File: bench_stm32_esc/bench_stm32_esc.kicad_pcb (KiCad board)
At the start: 4 copper layers, 117 x 75 mm, 107 parts, among them CN1 S6B-PH-K-S-, CN10 Conn_02x19_Odd_Even, CN7 Conn_02x19_Odd_Even, J1 XT60PW-M, Q1 CSD19532Q5B, Q2 CSD19532Q5B, Q3 CSD19532Q5B, Q4 CSD19532Q5B, Q5 CSD19532Q5B, Q6 CSD19532Q5B, U1 DRV8353RSRGZT, U2 AMS1117, U3 TPD1E05U06DYA, U4 MR60PW-M.G.B, U7 TB60

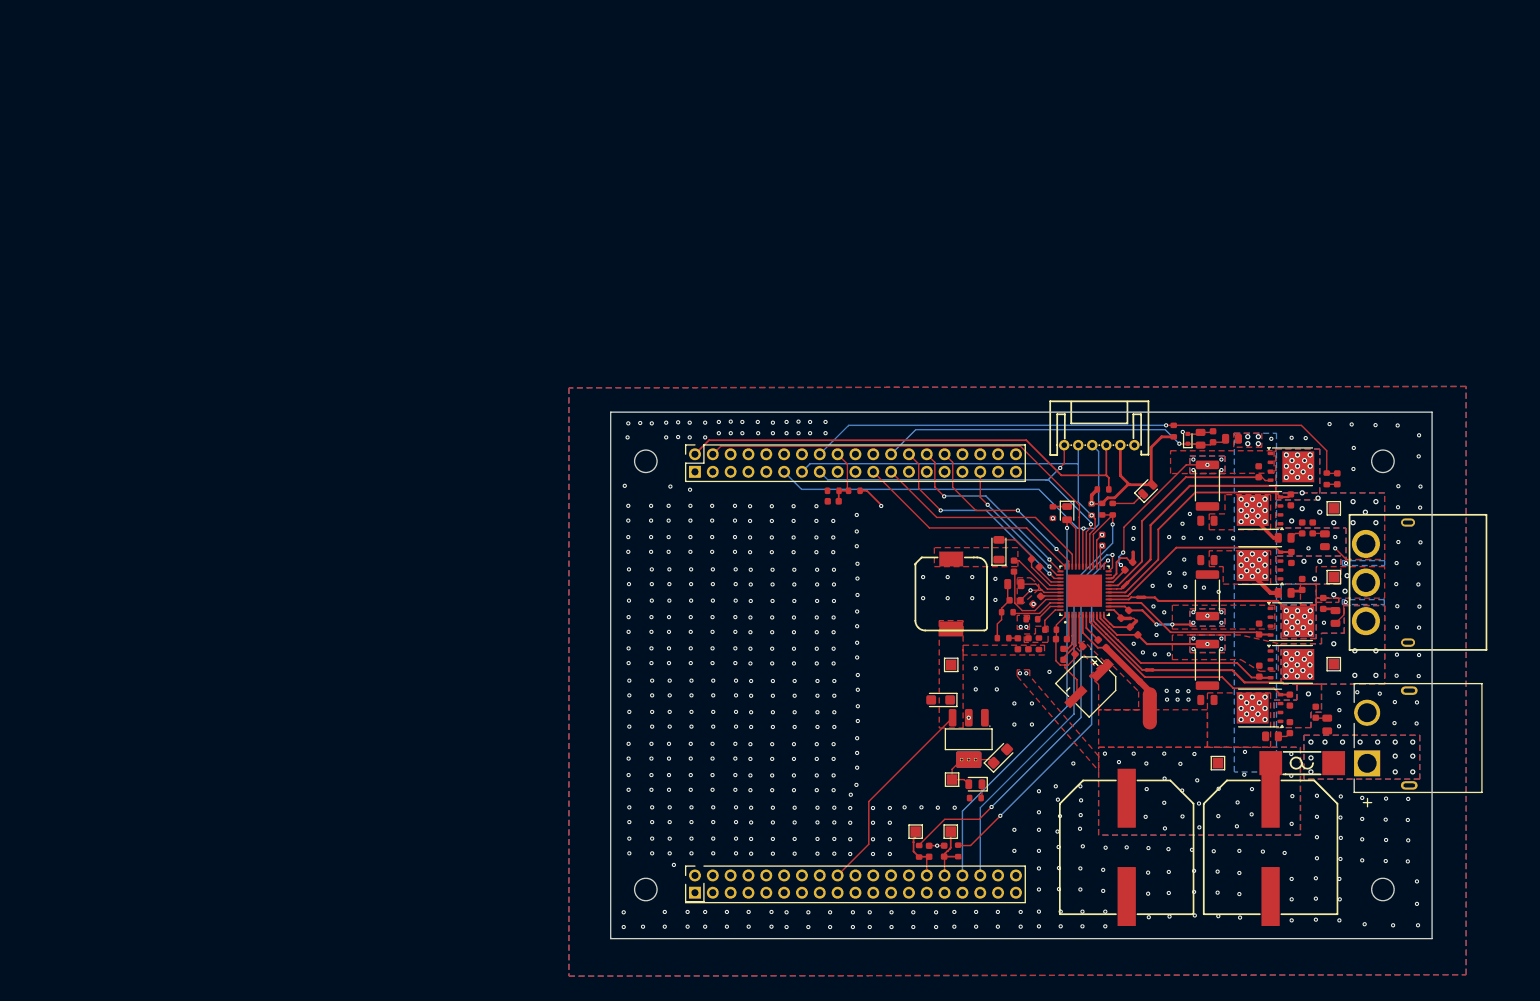
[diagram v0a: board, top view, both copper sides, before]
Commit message: Added smd stm32
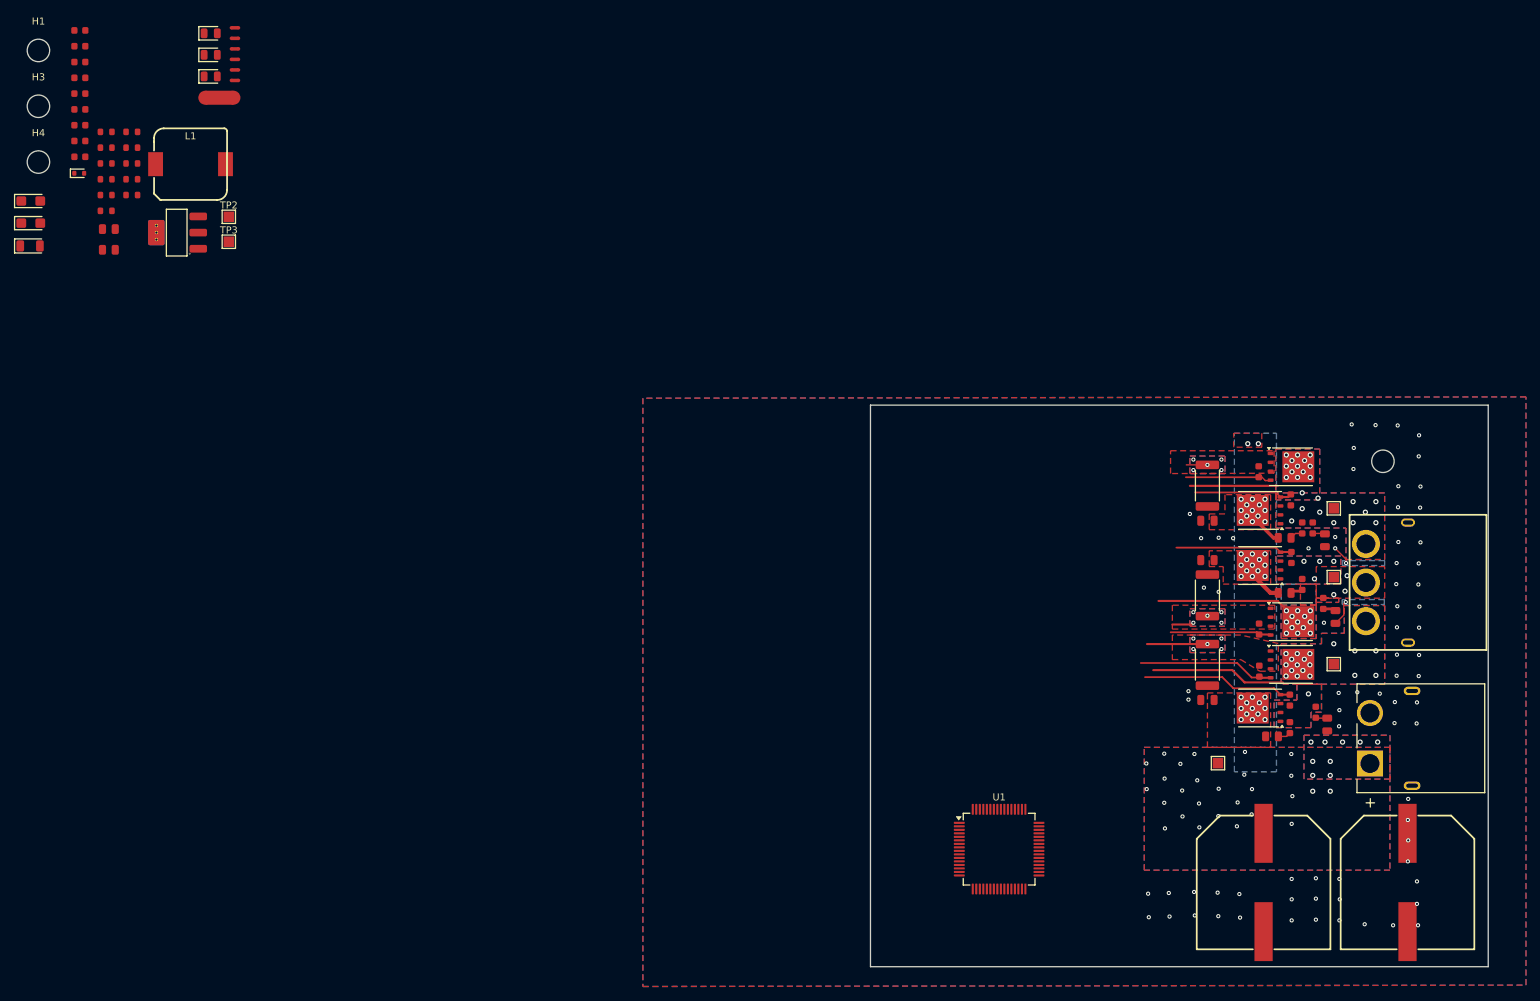
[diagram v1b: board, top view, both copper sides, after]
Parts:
- removed C1, C2, C3, C4: 1uF, PCM_JLCPCB:C_0603
- removed C16: VT10UF100V167RV0127, footprints:VT10UF100V167RV0127
- removed C34, C35: 2.2nF, PCM_JLCPCB:C_0603
- removed C5, C8, C9: 100nF, PCM_JLCPCB:C_0603
- removed C6: 47nF, PCM_JLCPCB:C_0603
- removed C7: 1uF, PCM_JLCPCB:C_0805
- removed CN1: S6B-PH-K-S-, footprints:S6B-PH-K-S(LF)(SN)
- removed CN10, CN7: Conn_02x19_Odd_Even, Connector_PinSocket_2.54mm:PinSocket_2x19_P2.54mm_Vertical
- removed R1: 100kΩ, PCM_JLCPCB:R_0603
- removed R15, R16: 56Ω, PCM_JLCPCB:R_0603
- removed R17: 1kΩ, PCM_JLCPCB:R_0603
- removed R2: 274kΩ, PCM_JLCPCB:R_0603
- removed R25: 10kΩ, PCM_JLCPCB:R_0603
- removed TP4, TP5: TestPoint, TestPoint:TestPoint_Pad_1.5x1.5mm
- removed U7: TB60, footprints:TB60
- U1: value DRV8353RSRGZT -> STM32G474RETx; footprint footprints:QFN50P700X700X100-49N -> Package_QFP:LQFP-64_10x10mm_P0.5mm
- moved H3 221.7 mm to (3.48, 11.4)
- moved C39 185.5 mm to (9.38, 16.4), turned to 0 degrees
- moved TH1 175.5 mm to (16.8, 21.8), turned to 0 degrees
- moved C21 169.6 mm to (9.38, 7.38), turned to 0 degrees
- moved C38 167.4 mm to (9.38, 14.1), turned to 0 degrees
- moved C24 166.3 mm to (9.38, 9.62), turned to 0 degrees
- moved C30 163.0 mm to (9.38, 11.9), turned to 0 degrees
- moved R18 162.8 mm to (13.5, 28.9), turned to 0 degrees
- moved U3 162.4 mm to (9.29, 21.0), turned to 0 degrees
- moved C12 159.7 mm to (9.38, 2.88), turned to 0 degrees
- moved NT1 159.2 mm to (31.5, 0.25)
- moved NT7 158.5 mm to (29.2, 10.2), turned to 0 degrees
- moved R19 157.8 mm to (13.5, 31.9), turned to 0 degrees
- moved C15 157.6 mm to (2.38, 28.1), turned to 0 degrees
- moved C14 157.2 mm to (9.38, 5.12), turned to 0 degrees
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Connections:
- J1 pad 1: Net-(J1-P) -> VM
- U1 pad 1: GND -> unconnected-(U1-VBAT-Pad1)
- U1 pad 10: /GLA -> unconnected-(U1-PC2-Pad10)
- U1 pad 11: /SPA -> unconnected-(U1-PC3-Pad11)
- U1 pad 12: /SNA -> unconnected-(U1-PA0-Pad12)
- U1 pad 13: /SNB -> unconnected-(U1-PA1-Pad13)
- U1 pad 14: /SPB -> unconnected-(U1-PA2-Pad14)
- U1 pad 15: /GLB -> Net-(U1-VSS-Pad15)
- U1 pad 16: /SHB -> unconnected-(U1-VDD-Pad16)
- U1 pad 17: /GHB -> unconnected-(U1-PA3-Pad17)
- U1 pad 18: /GHC -> unconnected-(U1-PA4-Pad18)
- U1 pad 19: /SHC -> unconnected-(U1-PA5-Pad19)
- U1 pad 2: Net-(U1-VGLS) -> unconnected-(U1-PC13-Pad2)
- U1 pad 20: /GLC -> unconnected-(U1-PA6-Pad20)
- U1 pad 21: /SPC -> unconnected-(U1-PA7-Pad21)
- U1 pad 22: /SNC -> unconnected-(U1-PC4-Pad22)
- U1 pad 24: Net-(U1-SOB) -> unconnected-(U1-PB0-Pad24)
- U1 pad 25: Net-(U1-SOA) -> unconnected-(U1-PB1-Pad25)
- U1 pad 26: +3V3 -> unconnected-(U1-PB2-Pad26)
- U1 pad 27: GND -> unconnected-(U1-VSSA-Pad27)
- U1 pad 28: /FAULT -> unconnected-(U1-VREF+-Pad28)
- U1 pad 29: /SPI_MISO -> unconnected-(U1-VDDA-Pad29)
- U1 pad 3: Net-(U1-CPL) -> unconnected-(U1-PC14-Pad3)
- U1 pad 30: /SPI_MOSI -> unconnected-(U1-PB10-Pad30)
- U1 pad 31: /SPI_SCK -> Net-(U1-VSS-Pad15)
- U1 pad 32: /GD_CS -> unconnected-(U1-VDD-Pad32)
- U1 pad 33: /ENABLE -> unconnected-(U1-PB11-Pad33)
- U1 pad 34: /INHA -> unconnected-(U1-PB12-Pad34)
- U1 pad 35: /INLA -> unconnected-(U1-PB13-Pad35)
- U1 pad 36: /INHB -> unconnected-(U1-PB14-Pad36)
- U1 pad 37: /INLB -> unconnected-(U1-PB15-Pad37)
- U1 pad 38: /INHC -> unconnected-(U1-PC6-Pad38)
- U1 pad 39: /INLC -> unconnected-(U1-PC7-Pad39)
- U1 pad 4: Net-(U1-CPH) -> unconnected-(U1-PC15-Pad4)
- U1 pad 40: Net-(U1-DVDD) -> unconnected-(U1-PC8-Pad40)
- U1 pad 41: GND -> unconnected-(U1-PC9-Pad41)
- U1 pad 42: /SW -> unconnected-(U1-PA8-Pad42)
- U1 pad 43: VM -> unconnected-(U1-PA9-Pad43)
- U1 pad 44: Net-(U1-VCC) -> unconnected-(U1-PA10-Pad44)
- U1 pad 45: /BST -> unconnected-(U1-PA11-Pad45)
- U1 pad 46: Net-(U1-RCL) -> unconnected-(U1-PA12-Pad46)
- U1 pad 47: Net-(U1-RT/SD) -> Net-(U1-VSS-Pad15)
- U1 pad 48: /FB -> unconnected-(U1-VDD-Pad48)
- U1 pad 49: GND -> unconnected-(U1-PA13-Pad49)
- U1 pad 5: VM -> unconnected-(U1-PF0-Pad5)
- U1 pad 6: /VDRAIN -> unconnected-(U1-PF1-Pad6)
- U1 pad 7: Net-(U1-VCP) -> unconnected-(U1-PG10-Pad7)
- U1 pad 8: /GHA -> unconnected-(U1-PC0-Pad8)
- U1 pad 9: /SHA -> unconnected-(U1-PC1-Pad9)
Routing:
- net /PHASE_TMP: track 80.1 -> 0.00 mm, vias 1 -> 0
- net /FAULT: track 69.2 -> 0.00 mm, vias 1 -> 0
- net /ENC_CS: track 68.0 -> 0.00 mm
- net /SPI_SCK: track 65.5 -> 0.00 mm, vias 1 -> 0
- net /GD_CS: track 64.9 -> 0.00 mm
- net /ENABLE: track 64.0 -> 0.00 mm, vias 1 -> 0
- net Net-(U1-SOB): track 58.7 -> 0.00 mm, vias 2 -> 0
- net /SPI_MISO: track 58.5 -> 0.00 mm, vias 1 -> 0
- net /SPI_MOSI: track 54.4 -> 0.00 mm, vias 2 -> 0
- net Net-(U1-SOA): track 52.0 -> 0.00 mm, vias 2 -> 0
- net /VSENVM: track 50.1 -> 0.00 mm, vias 1 -> 0
- net GND: track 55.2 -> 6.38 mm, vias 547 -> 76
- net +3V3: track 43.8 -> 0.00 mm, vias 4 -> 0
- net /INHB: track 32.9 -> 0.00 mm
- net /INHA: track 32.4 -> 0.00 mm
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- removed copper zone on In2.Cu, net +3V3
- removed copper zone on F.Cu, net /FB
- removed copper zone on F.Cu, net /SW
- removed copper zone on B.Cu, net Net-(J1-P)
- removed copper zone on F.Cu, net Net-(J1-P)
- removed copper zone on In1.Cu, net Net-(J1-P)
- removed copper zone on In2.Cu, net Net-(J1-P)
- removed copper zone on F.Cu, net VBUCK
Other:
- board size 117 x 75 mm -> 88 x 80 mm

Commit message: New gate drivers
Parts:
- removed C24, C30: 1nF, PCM_JLCPCB:C_0603
- removed C33: 2.2nF, PCM_JLCPCB:C_0603
- removed C38: 47nF, PCM_JLCPCB:C_0603
- removed C40: 100nF, PCM_JLCPCB:C_0603
- removed D4: Red, PCM_JLCPCB:D_0805
- removed D6: Yellow, PCM_JLCPCB:D_0805
- removed H4: MountingHole, MountingHole:MountingHole_3.2mm_M3
- removed L1: SMDRH104R-331MT, footprints:SMDRH104R-331MT
- removed NT1, NT2, NT3, NT4, NT5, NT6: NetTie_2, NetTie:NetTie-2_SMD_Pad0.5mm
- removed NT7: NetTie_2, NetTie:NetTie-2_SMD_Pad2.0mm
- removed Q3, Q4, Q5, Q6: CSD19532Q5B, Package_TO_SOT_SMD:TDSON-8-1
- removed R14, R7: 2.7Ω, PCM_JLCPCB:R_0805
- removed R18: 383kΩ, PCM_JLCPCB:R_0805
- removed R26, R27, R28: 330Ω, PCM_JLCPCB:R_0603
- removed R9: 7mΩ, Resistor_SMD:R_2512_6332Metric
- removed TP3, TP6, TP7, TP8: TestPoint, TestPoint:TestPoint_Pad_1.5x1.5mm
- removed U2: AMS1117, PCM_JLCPCB:SOT-223-3_L6.5-W3.4-P2.30-LS7.0-BR
- removed U3: TPD1E05U06DYA, PCM_JLCPCB:D_SOD-523
- added C1: 10pF, PCM_JLCPCB:C_0603, F.Cu at (118.7, 78.6)
- added C16: 100nF, PCM_JLCPCB:C_0603, F.Cu at (122.5, 89.9)
- added C2: 2.2uF, PCM_JLCPCB:C_0603, F.Cu at (118.7, 80.9)
- added C3: 100nF, PCM_JLCPCB:C_0603, F.Cu at (118.7, 83.1)
- added C34: 58pF, PCM_JLCPCB:C_0603, F.Cu at (130.2, 78.6)
- added C4: 10pF, PCM_JLCPCB:C_0603, F.Cu at (118.7, 85.4)
- added C41: 22uF, PCM_JLCPCB:C_0603, F.Cu at (130.2, 87.6)
- added C42: 2.2uF, PCM_JLCPCB:C_0603, F.Cu at (130.2, 89.9)
- added C44: 22uF, PCM_JLCPCB:C_0603, F.Cu at (130.2, 92.1)
- added C45: 100nF, PCM_JLCPCB:C_0603, F.Cu at (130.2, 94.4)
- added C46: 100nF, PCM_JLCPCB:C_0603, F.Cu at (130.2, 96.6)
- added C5: 100nF, PCM_JLCPCB:C_0603, F.Cu at (118.7, 87.6)
- added C6: 1uF, PCM_JLCPCB:C_0603, F.Cu at (118.7, 89.9)
- added C7: 2.2nF, PCM_JLCPCB:C_0603, F.Cu at (118.7, 92.1)
- added C8: 2.2nF, PCM_JLCPCB:C_0603, F.Cu at (118.7, 94.4)
- added C9: 1uF, PCM_JLCPCB:C_0603, F.Cu at (118.7, 96.6)
- added FB1: ~, PCM_JLCPCB:FB_0603, F.Cu at (129.2, 99.0)
- added FB2: ~, PCM_JLCPCB:FB_0603, F.Cu at (129.2, 101.5)
- added J2: XT60PW-M, footprints:AMASS_XT60PW-M, F.Cu at (187.2, 104.2)
- added L2: SM7850-680MT, footprints:SM7850-680MT, F.Cu at (122.0, 102.3)
- added R1: 3.3Ω, PCM_JLCPCB:R_0603, F.Cu at (141.9, 93.1)
- added R15: 150kΩ, PCM_JLCPCB:R_0603, F.Cu at (145.6, 93.1)
- added R16: 5.1kΩ, PCM_JLCPCB:R_0603, F.Cu at (145.6, 95.3)
- added R17: 5.1kΩ, PCM_JLCPCB:R_0603, F.Cu at (145.6, 97.6)
- added R23: 330Ω, PCM_JLCPCB:R_0603, F.Cu at (149.2, 93.1)
- added R25: 4.7kΩ, PCM_JLCPCB:R_0603, F.Cu at (149.2, 97.6)
- added R34: 2.7Ω, PCM_JLCPCB:R_0805, F.Cu at (134.4, 114.6)
- added U10: AS5047D, Package_SO:TSSOP-14_4.4x5mm_P0.65mm, F.Cu at (121.1, 110.3)
- added U11: USBLC6-2P6, Package_TO_SOT_SMD:SOT-666, F.Cu at (129.2, 104.6)
- added U12: MR60PW-M.G.B, footprints:CONN-TH_MR60PW, F.Cu at (183.8, 85.8)
- added U5: INA240A2D, Package_SO:SOIC-8_3.9x4.9mm_P1.27mm, F.Cu at (155.3, 95.3)
- added U6: STM32G474RETx, Package_QFP:LQFP-64_10x10mm_P0.5mm, F.Cu at (147.3, 84.7)
- added U8: LM5164DDA, Package_SO:HSOP-8-1EP_3.9x4.9mm_P1.27mm_EP2.41x3.1mm_ThermalVias, F.Cu at (155.3, 101.9)
- added U9: TPD1E05U06DYA, PCM_JLCPCB:D_SOD-523, F.Cu at (134.0, 117.3)
- added X1: X322516MLB4SI, PCM_JLCPCB:OSC-SMD_4P-L3.2-W2.5-BL, F.Cu at (128.1, 116.1)
- C11: value 10nF -> 2.2nF
- C12: value 3.3nF -> 2.2nF
- C13: value 10uF -> 100nF; footprint PCM_JLCPCB:C_CASE-A-3216-18(mm) -> PCM_JLCPCB:C_0603
- C14: value 2.2uF -> 10uF
- C15: value 22uF -> 100nF; footprint PCM_JLCPCB:C_CASE-A-3216-18(mm) -> PCM_JLCPCB:C_0603
- C17, C18, C19, C20, C23, C28: value 2.2nF -> 100nF
- C21: value 1nF -> 100nF
- C22, C26: value 2.2nF -> 1uF
- C25: value 1uF -> 2.2uF; footprint PCM_JLCPCB:C_0805 -> PCM_JLCPCB:C_0603
- C27: value 2.2nF -> 47nF
- C29, C32: value 2.2nF -> VEJ331M2ATR-1816; footprint PCM_JLCPCB:C_0603 -> footprints:VEJ331M2ATR-1816
- C31: value 1uF -> 2.2nF; footprint PCM_JLCPCB:C_0805 -> PCM_JLCPCB:C_0603
- C36: value VEJ331M2ATR-1816 -> 2.2nF; footprint footprints:VEJ331M2ATR-1816 -> PCM_JLCPCB:C_0603
- C37: value VEJ331M2ATR-1816 -> 2.2uF; footprint footprints:VEJ331M2ATR-1816 -> PCM_JLCPCB:C_0603
- C39: value 100nF -> 22uF
- D1: value DSK120 -> Green; footprint PCM_JLCPCB:D_SOD-123FL -> PCM_JLCPCB:D_0805
- D2: value Green -> Yellow
- J1: value XT60PW-M -> USB_C_Receptacle_USB2.0_16P; footprint footprints:AMASS_XT60PW-M -> Connector_USB:USB_C_Receptacle_HRO_TYPE-C-31-M-12
- R10: value 2.7Ω -> 100kΩ; footprint PCM_JLCPCB:R_0805 -> PCM_JLCPCB:R_0603
- R11: value 2.7Ω -> 383kΩ
- R12: value 7mΩ -> 9.76kΩ; footprint Resistor_SMD:R_2512_6332Metric -> PCM_JLCPCB:R_0805
- R13, R6: value 2.7Ω -> 10kΩ; footprint PCM_JLCPCB:R_0805 -> PCM_JLCPCB:R_0603
- R19: value 9.76kΩ -> 360kΩ; footprint PCM_JLCPCB:R_0805 -> PCM_JLCPCB:R_0603
- R21: value 4.7kΩ -> 470kΩ
- R22: value 4.7kΩ -> 330Ω
- R24: value 10kΩ -> 4.7kΩ
- R3: value 10kΩ -> 3.3Ω
- R4: value 10kΩ -> 2.7Ω; footprint PCM_JLCPCB:R_0603 -> PCM_JLCPCB:R_0805
- R5: value 2.2Ω -> 2.7Ω; footprint PCM_JLCPCB:R_0603 -> PCM_JLCPCB:R_0805
- R8: value 7mΩ -> 330kΩ; footprint Resistor_SMD:R_2512_6332Metric -> PCM_JLCPCB:R_0603
- U1: value STM32G474RETx -> UCC27211ADRMR; footprint Package_QFP:LQFP-64_10x10mm_P0.5mm -> easyeda2kicad:VSON-8_L4.0-W4.0-P0.80-TL-EP
- U4: value MR60PW-M.G.B -> AP2112K-3.3; footprint footprints:CONN-TH_MR60PW -> Package_TO_SOT_SMD:SOT-23-5
- moved H1 198.7 mm to (194.2, 59.0)
- moved D1 161.7 mm to (156.8, 79.0)
- moved H3 158.1 mm to (136.1, 97.4)
- moved R21 154.9 mm to (145.6, 102.1)
- moved R22 154.9 mm to (145.6, 104.3)
- moved TH1 153.7 mm to (149.2, 99.8)
- moved TH2 153.7 mm to (149.2, 102.1)
- moved R24 152.6 mm to (149.2, 95.3)
- moved D2 152.2 mm to (156.8, 82.1)
- moved R3 151.8 mm to (141.9, 95.3)
- moved R5 148.8 mm to (134.4, 105.8)
- moved R19 148.5 mm to (145.6, 99.8)
- moved R4 148.3 mm to (134.4, 102.8)
- moved C39 139.2 mm to (130.2, 85.4)
- moved C14 138.7 mm to (122.5, 85.4)
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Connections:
- C11 pad 1: /BST -> Net-(C11-Pad1)
- C11 pad 2: /SW -> Net-(C11-Pad2)
- C12 pad 1: VBUCK -> Net-(C11-Pad2)
- C12 pad 2: /FB -> Net-(C12-Pad2)
- C13 pad 1: VBUCK -> /NRST
- C14 pad 1: VBUCK -> GND
- C14 pad 2: Net-(C14-Pad2) -> +3V3
- C17 pad 1: Net-(C17-Pad1) -> +3V3
- C17 pad 2: /MOTA -> GND
- C18 pad 1: /MOTA -> +3V3
- C18 pad 2: Net-(C18-Pad2) -> GND
- C19 pad 1: /GHA -> +3V3
- C19 pad 2: /MOTA -> GND
- C20 pad 1: /GLA -> +3V3
- C20 pad 2: /SPA -> GND
- C21 pad 1: /SPA -> +3V3A
- C21 pad 2: /SNA -> GND
- C22 pad 1: /GHB -> +3V3A
- C22 pad 2: /MOTB -> GND
- C23 pad 1: /GLB -> +3V3
- C23 pad 2: /SPB -> GND
- C26 pad 1: /MOTB -> +3V3
- C26 pad 2: Net-(C26-Pad2) -> GND
- C27 pad 1: Net-(C27-Pad1) -> /VSENVM
- C27 pad 2: /MOTB -> GND
- C28 pad 1: /GHC -> +3V3
- C28 pad 2: /MOTC -> GND
- C29 pad 1: /GLC -> VM
- C29 pad 2: /SPC -> GND
- C31 pad 1: VM -> /SW_12V
- C31 pad 2: GND -> Net-(U8-BST)
- C32 pad 1: /MOTC -> VM
- C32 pad 2: Net-(C32-Pad2) -> GND
- C36 pad 1: VM -> Net-(C34-Pad1)
- C36 pad 2: GND -> +12V_VM
- C37 pad 1: VM -> /USB_VBUS
- C39 pad 1: /PHASE_TMP -> +12V_VM
- D1 pad 1: /SW -> Net-(D1-Pad1)
- D1 pad 2: GND -> /ENABLE
- D2 pad 2: /ENABLE -> +3V3
- Q1 pad 1: /MOTA -> /MP_A
- Q1 pad 2: /MOTA -> /MP_A
- Q1 pad 3: /MOTA -> /MP_A
- Q2 pad 1: /SPA -> GND
- Q2 pad 2: /SPA -> GND
- Q2 pad 3: /SPA -> GND
- Q2 pad 5: /MOTA -> /MP_A
- R10 pad 1: Net-(C26-Pad2) -> /RON_12V
- R11 pad 2: Net-(C27-Pad1) -> /VSENVM
- R12 pad 1: /SPC -> /VSENVM
- R13 pad 1: Net-(C32-Pad2) -> +3V3
- R13 pad 2: GND -> Net-(U10-~{CS})
- R19 pad 1: /VSENVM -> /SW_12V
- R19 pad 2: GND -> Net-(C34-Pad1)
- R21 pad 1: +3V3 -> /FB_12V
- R21 pad 2: /PHASE_TMP -> +12V_VM
- R22 pad 1: +3V3 -> Net-(D1-Pad1)
- R22 pad 2: /AMBIENT_TMP -> GND
- R24 pad 2: /ENC_CS -> /PHASE_TMP
- R3 pad 1: VBUCK -> Net-(U1-HO)
- R3 pad 2: /FB -> /GHA
- R4 pad 1: /FB -> VM
- R4 pad 2: GND -> Net-(C11-Pad1)
- R5 pad 1: Net-(C14-Pad2) -> Net-(C12-Pad2)
- R6 pad 1: VM -> /BOOT0
- R6 pad 2: Net-(C17-Pad1) -> /SW_BOOT0
- R8 pad 1: /SPA -> /EN_12V
- TH2 pad 1: /AMBIENT_TMP -> /AMB_TMP
- TP1 pad 1: VM -> /MP_A
- TP2 pad 1: VBUCK -> VM
- U1 pad 1: unconnected-(U1-VBAT-Pad1) -> +12V_VM
- U1 pad 2: unconnected-(U1-PC13-Pad2) -> Net-(U1-HB)
- U1 pad 3: unconnected-(U1-PC14-Pad3) -> Net-(U1-HO)
- U1 pad 4: unconnected-(U1-PC15-Pad4) -> Net-(U1-HS)
- U1 pad 5: unconnected-(U1-PF0-Pad5) -> /PWM_HA
- U1 pad 6: unconnected-(U1-PF1-Pad6) -> /PWM_LA
- U1 pad 7: unconnected-(U1-PG10-Pad7) -> GND
- U1 pad 8: unconnected-(U1-PC0-Pad8) -> Net-(U1-LO)
- U1 pad 9: unconnected-(U1-PC1-Pad9) -> GND
- U4 pad 1: /MOTA -> +5V_USB
- U4 pad 2: /MOTB -> GND
- U4 pad 3: /MOTC -> +5V_USB
- U4 pad 4: GND -> unconnected-(U4-NC-Pad4)
- U4 pad 5: GND -> +3V3
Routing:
- net /GHA: track 21.7 -> 0.00 mm
- net /MOTB: track 21.1 -> 0.00 mm, vias 20 -> 0
- net /GLA: track 19.7 -> 0.00 mm
- net /MOTA: track 19.2 -> 0.00 mm, vias 19 -> 0
- net /GHB: track 16.6 -> 0.00 mm
- net /GLB: track 14.3 -> 0.00 mm
- net /GHC: track 14.0 -> 0.00 mm
- net /MOTC: track 12.5 -> 0.00 mm, vias 24 -> 0
- net /GLC: track 12.2 -> 0.00 mm
- net VM: track 9.56 -> 0.00 mm, vias 77 -> 0
- net /SPA: track 8.62 -> 0.00 mm, vias 5 -> 0
- net GND: track 6.38 -> 0.00 mm, vias 76 -> 0
- net /SPB: track 3.10 -> 0.00 mm, vias 5 -> 0
- net /SPC: track 3.01 -> 0.00 mm, vias 5 -> 0
- net Net-(C33-Pad1): track 1.85 -> 0.00 mm
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- removed copper zone on B.Cu, net /MOTA
- removed copper zone on F.Cu, net /MOTA
- removed copper zone on In1.Cu, net /MOTA
- removed copper zone on In2.Cu, net /MOTA
- removed copper zone on B.Cu, net /MOTB
- removed copper zone on F.Cu, net /MOTB
- removed copper zone on In1.Cu, net /MOTB
- removed copper zone on In2.Cu, net /MOTB
- removed copper zone on B.Cu, net /MOTC
- removed copper zone on F.Cu, net /MOTC
- removed copper zone on In1.Cu, net /MOTC
- removed copper zone on In2.Cu, net /MOTC
- removed copper zone on B.Cu, net /SPA
- removed copper zone on F.Cu, net /SPA
- removed copper zone on In1.Cu, net /SPA
- removed copper zone on In2.Cu, net /SPA
- removed copper zone on B.Cu, net /SPB
- removed copper zone on F.Cu, net /SPB
- removed copper zone on In1.Cu, net /SPB
- removed copper zone on In2.Cu, net /SPB
- removed copper zone on B.Cu, net /SPC
- removed copper zone on F.Cu, net /SPC
- removed copper zone on In1.Cu, net /SPC
- removed copper zone on In2.Cu, net /SPC
- removed copper zone on B.Cu, net VM
- removed copper zone on F.Cu, net VM
- removed copper zone on In1.Cu, net VM
- removed copper zone on In2.Cu, net VM
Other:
- board size 88 x 80 mm -> 80 x 80 mm
- board text removed: "Q1"
